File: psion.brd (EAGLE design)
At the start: 161.7 x 81.5 mm, 94 parts, among them J2 1-2295018-2, Q2 NTF3055L108T1G, Q3 NTF3055L108T1G, Q5 MOSFET-PCH_SOT-223, Q6 MOSFET-PCH_SOT-223, Q8 MMBT2907ALT1G, T1 2908-05WB-MG, U2 HV823LG-G, U3 ATMEGA32U4-AU, U4 OSD3358-512M-BCB, U5 MAX1620EEE+, U6 MAX1620EEE+, U7 ATTINY404-SSN, U8 TPS61090RSAR, Y1 ABM10-16.000MHZ-D30-T3

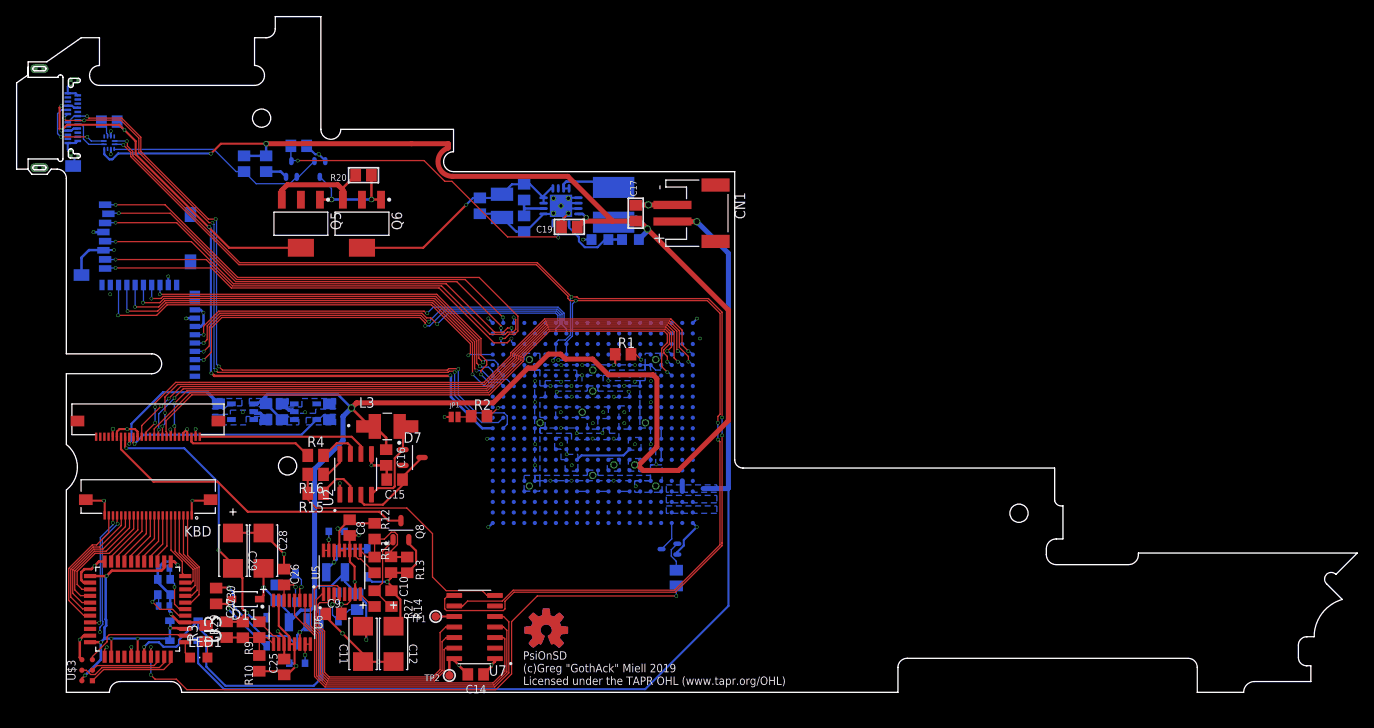
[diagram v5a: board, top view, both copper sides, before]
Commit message: Added audio compoments, massive board changes to accommodate physical space & rf restrictions
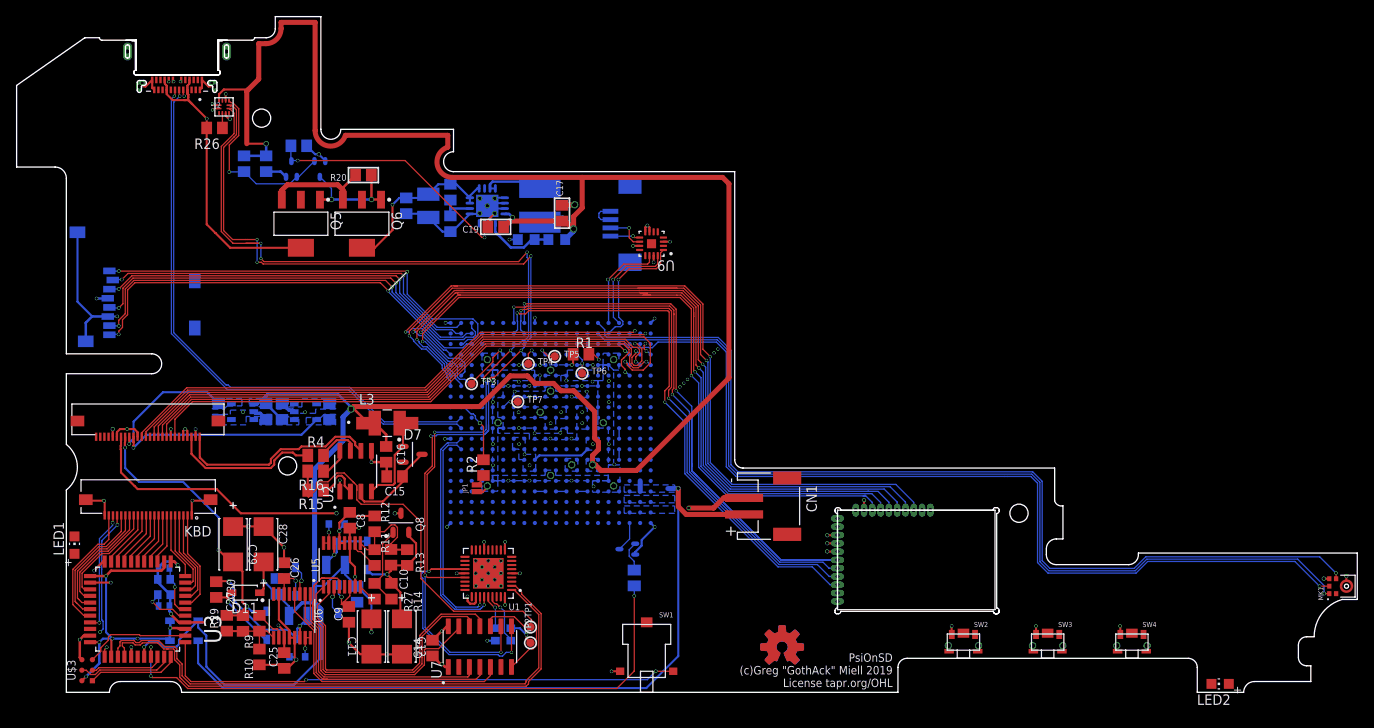
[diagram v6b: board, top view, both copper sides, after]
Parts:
- removed R3: 1k, adafruit:M0805
- added J1: 0522070433, gothack:MOLEX_0522070433
- added LED2: (no value), adafruit:CHIP-LED0805
- added MK1: SPH0645LM4H-B, gothack:MIC_SPH0645LM4H-B
- added SW1: KSM1131, gothack:KSM1131
- added SW2, SW3, SW4: LS12T2-T, gothack:LS12T2-T
- added TP3, TP4, TP5, TP6, TP7: (no value), microbuilder:TESTPOINT_ROUND_1MM
- added U1: USB2514BI-AEZG, USB2514BI-AEZG:QFN50P600X600X100-37N
- added U9: MAX98357AETE+, MAX98357AETE_:QFN50P300X300X80-17N
- added Y2: ABM10-24.000MHZ-E20-T, ABM10-16.000MHZ-D30-T3:XTAL250X200X50
- J2: device 1-2295018-2:TE_1-2295018-2 -> gothack:TE_1-2295018-2
- LED1: device adafruit:CHIPLED_0805 -> adafruit:CHIP-LED0805
- U$1: value LM832 -> LM832EMBEDDED; device LM832:LM832SMT -> gothack:LM832SMT_EMB
- moved U$1 82.1 mm to (99.0, 22.0), flipped to the top
- moved CN1 36.4 mm to (91.4, 22.5)
- moved U$5 28.5 mm to (92.3, 5.46)
- moved U$7 28.5 mm to (92.3, 5.46)
- moved LED1 20.2 mm to (6.99, 17.8), turned to 0 degrees
- moved J2 18.4 mm to (19.4, 77.3), flipped to the top, turned to 180 degrees
- moved U$4 14.5 mm to (25.0, 70.6), flipped to the top, turned to 0 degrees
- moved R26 12.7 mm to (23.9, 68.1), flipped to the top
- moved TP1 11.5 mm to (62.0, 7.87), turned to 90 degrees
- moved TP2 10.5 mm to (62.0, 5.97), turned to 90 degrees
- moved JP1 9.01 mm to (55.5, 24.6), turned to 90 degrees
- moved U8 8.89 mm to (56.8, 58.7)
- moved C17 8.89 mm to (65.8, 57.8)
- moved C18 8.89 mm to (47.0, 58.7)
- moved C19 8.89 mm to (57.8, 56.1)
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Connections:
- net LCD_BIASN_DN renamed LCD_BIASND_N
- net LCD_BIASP_DN renamed LCD_BIASPD_N
- net U0_CTS renamed UART0_CTS
- net U0_RTS renamed UART0_RTS
- net U0_RXD renamed UART0_RXD
- net U0_TXD renamed UART0_TXD
- net USBC_DN renamed USBCD_N
- net USBC_DP renamed USBCD_P
- removed net KBD_USB_DN: U3.3
- removed net KBD_USB_DP: U3.4
- removed net U1_CTS: U$1.P$18, U4.W8
- removed net U1_RTS: U$1.P$16, U4.Y8
- removed net U1_RXD: U$1.P$17, U4.Y7
- removed net U1_TXD: U$1.P$19, U4.W7
- removed net USB1_DN: U4.H2
- removed net USB1_DP: U4.J2
- new net AIN0: U4.Y10
- new net AIN1: U4.W10
- new net AIN2: U4.V10
- new net AIN3: U4.V9
- new net AIN4: U4.Y11
- new net AIN5: U4.W11
- new net AIN6: U4.V11
- new net AIN7: U4.V12
- new net ECAP0_IN_PWM0_OUT: U4.V15
- new net EMMC_RSTN: U4.A4
- new net EMU0: U4.V18
- new net EMU1: U4.V19
- new net EP: U9.17
- new net GPMC_A0: U4.A13
- new net GPMC_A1: U4.B13
- new net GPMC_A10: U4.B10
- new net GPMC_A11: U4.C10
- new net GPMC_A2: U4.C13
- new net GPMC_A3: U4.A12
- new net GPMC_A4: U4.B12
- new net GPMC_A5: U4.C12
- new net GPMC_A6: U4.A11
- new net GPMC_A7: U4.B11
- new net GPMC_A8: U4.C11
- new net GPMC_A9: U4.A10
- new net GPMC_AD10: U4.B16
- new net GPMC_AD11: U4.A16
- new net GPMC_AD12: U4.C15
- new net GPMC_AD13: U4.B15
- new net GPMC_AD14: U4.A15
- new net GPMC_AD15: U4.C14
- new net GPMC_AD8: U4.A17
- new net GPMC_AD9: U4.C16
- new net GPMC_ADVN_ALE: U4.L19
- new net GPMC_BEN0_CLE: U4.L20
- new net GPMC_BEN1: U4.C9
- new net GPMC_CLK: U4.A14
- new net GPMC_CSN0: U4.K20
- new net GPMC_CSN3: U4.B14
- new net GPMC_OEN_REN: U4.K19
- new net GPMC_WAIT0: U4.B9
- new net GPMC_WEN: U4.K18
- new net GPMC_WPN: U4.A9
- new net KBD_USBD_N: U1.1, U3.3
- new net KBD_USBD_P: U1.2, U3.4
- new net MCASP0_ACLKR: MK1.4, U4.Y15
- new net MCASP0_ACLKX: U4.Y17, U9.16
- new net MCASP0_AHCLKR: U4.W17
- new net MCASP0_AHCLKX: U4.V16
- new net MCASP0_AXR0: U4.W16, U9.1
- new net MCASP0_AXR1: MK1.6, U4.V17
- new net MCASP0_FSR: MK1.1, U4.W15
- new net MCASP0_FSX: U4.Y16, U9.14
- new net N$15: U1.32, Y2.3
- new net N$17: TP5.P$1, U4.U10
- new net N$18: TP6.P$1, U4.U13
- new net N$19: TP7.P$1, U4.M6
- new net N$20: J1.1, J1.2
- new net N$21: U3.6
- new net N$4: U1.33, Y2.1
- new net NC0: U4.A2
- new net NC1: U4.A3
- new net NC10: U4.B5
- new net NC11: U4.B6
- new net NC12: U4.B7
- new net NC13: U4.B8
- new net NC14: U4.C1
- new net NC15: U4.C2
- new net NC16: U4.C3
- new net NC17: U4.C4
- new net NC18: U4.C5
- new net NC19: U4.C6
- new net NC2: U4.A5
- new net NC20: U4.C7
- new net NC21: U4.C8
- new net NC22: U4.D1
- new net NC23: U4.D2
- new net NC24: U4.D3
- new net NC25: U4.D6
- new net NC26: U4.D7
- new net NC27: U4.D8
- new net NC28: U4.E1
- new net NC29: U4.E2
- new net NC3: U4.A6
- new net NC30: U4.E3
- new net NC31: U4.E18
- new net NC32: U4.F1
- new net NC33: U4.F2
- new net NC34: U4.F3
- new net NC35: U4.F4
- new net NC36: U4.F6
- new net NC37: U4.F7
- new net NC38: U4.F20
- new net NC39: U4.G1
- new net NC4: U4.A7
- new net NC40: U4.G2
- new net NC41: U4.U11
- new net NC42: U4.R17
- new net NC43: U4.R15
- new net NC44: U4.R14
- new net NC45: U4.R8
- new net NC46: U4.R7
- new net NC47: U4.R6
- new net NC48: U4.R4
- new net NC49: U4.P17
- new net NC5: U4.A8
- new net NC50: U4.P4
- new net NC51: U4.N17
- new net NC52: U4.N4
- new net NC53: U4.M17
- new net NC54: U4.M4
- new net NC55: U4.L17
- new net NC56: U4.L4
- new net NC57: U4.K4
- new net NC58: U4.J20
- new net NC59: U4.J19
- new net NC6: U4.B1
- new net NC60: U4.J18
- new net NC61: U4.J6
- new net NC62: U4.J4
- new net NC63: U4.H20
- new net NC64: U4.H19
- new net NC65: U4.H18
- new net NC66: U4.H13
- new net NC67: U4.H12
- new net NC68: U4.H11
- new net NC69: U4.H10
- new net NC7: U4.B2
- new net NC70: U4.H9
- new net NC71: U4.H6
- new net NC72: U4.H4
- new net NC73: U4.G20
- new net NC74: U4.G19
- new net NC75: U4.G18
- new net NC76: U4.G11
- new net NC77: U4.G10
- new net NC78: U4.G7
- new net NC79: U4.G6
- new net NC8: U4.B3
- new net NC80: U4.G4
- new net NC81: U4.G3
- new net NC9: U4.B4
- new net OSC0_CTL: U4.M1
- new net OSC1_GND: U4.W13
- new net OSC1_IN: U4.Y13
- new net OSC1_OUT: U4.Y14
- new net PMIC_MUX_IN: U4.F19
- new net PMIC_MUX_OUT: U4.U12
- new net PMIC_NRESET: U4.A19
- new net PMIC_TS: U4.E20
- new net PWRONRSTN_OD: U4.C17
- new net S: J1.S1, J1.S2
- new net SPI0_CS0: U4.Y4
- new net SPI0_CS1: U4.V4
- new net SPI0_D0: U4.W5
- new net SPI0_D1: U4.W4
- new net SPI0_SCLK: U4.Y5
- new net SPKR_LN: J1.3, U9.10
- new net SPKR_LP: J1.4, U9.9
- new net SW_LID: SW1.2, U3.12
- new net SW_MEDIA1: SW2.2
- new net SW_MEDIA2: SW3.2
- new net SW_MEDIA3: SW4.2
- new net SYS_ADC_1P8V: U4.Y12
- new net SYS_VDD1_CTL: U4.F18
- new net TCK: U4.Y19
- new net TDI: U4.Y18
- new net TDO: U4.W18
- new net TMS: U4.W19
- new net TRSTN: U4.W20
- new net UART1_CTS: U$1.18, U4.W8
- new net UART1_RTS: U$1.16, U4.Y8
- new net UART1_RXD: U$1.17, U4.Y7
- new net UART1_TXD: U$1.19, U4.W7
- new net USB1D_N: U1.30, U4.H2
- new net USB1D_P: U1.31, U4.J2
- new net USB1_CE: U4.J3
- new net USB1_DRVVBUS: U4.H3
- new net USB1_VBUS: U4.H1
- new net USBC_CE: U4.L3
- new net USBC_DRVVBUS: U4.K3
- new net USB_DN2D_N: U1.3
- new net USB_DN2D_P: U1.4
- new net USB_DN3D_N: U1.6
- new net USB_DN3D_P: U1.7
- new net USB_DN4D_N: U1.8
- new net USB_DN4D_P: U1.9
- new net VDDS_RTC@2: U4.U14
- new net VREFN: U4.W9
- new net VREFP: U4.W12
- new net WARMRSTN: U4.B17
- new net XDMA_EVENT_INTR0: U4.W14
- new net XDMA_EVENT_INTR1: U4.V14
- net +3V3: now also MK1.5, U$1.14, U$1.9, U1.10, U1.15, U1.23, U1.29, U1.36, U1.5, U9.7, U9.8; no longer U$1.P$14, U$1.P$9
- net GND: now also MK1.3, SW1.1, SW2.1, SW3.1, SW4.1, U$1.13, U$1.15, U1.37, U4.Y9, U9.11, U9.15, U9.3, Y2.2, Y2.4; no longer R3.2, U$1.P$13, U$1.P$15
- net I2C0_SCL: now also U1.24
- net I2C0_SDA: now also U1.22
- net KBDAVR_VCC: no longer U3.6
- net N$2: now also TP3.P$1, U4.U6; no longer LED1.C, R3.1
- net N$6: now also TP4.P$1, U4.U9; no longer LED1.A, U3.12
- net SD1_CLK: now also U$1.3; no longer U$1.P$3
- net SD1_CMD: now also U$1.5; no longer U$1.P$5
- net SD1_D0: now also U$1.6; no longer U$1.P$6
- net SD1_D1: now also U$1.8; no longer U$1.P$8
- net SD1_D2: now also U$1.4; no longer U$1.P$4
- net SD1_D3: now also U$1.7; no longer U$1.P$7
- net USBC_ID: now also U4.L1
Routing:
- net MCASP0_ACLKR: track 0.00 -> 117.4 mm, vias 0 -> 1
- net MCASP0_FSR: track 0.00 -> 116.6 mm, vias 0 -> 1
- net MCASP0_AXR1: track 0.00 -> 113.3 mm, vias 0 -> 1
- net UART1_RTS: track 0.00 -> 93.2 mm, vias 0 -> 2
- net KBD_USBD_P: track 0.00 -> 69.1 mm
- net KBD_USBD_N: track 0.00 -> 68.3 mm
- net UART1_TXD: track 0.00 -> 66.0 mm, vias 0 -> 2
- net UART1_CTS: track 0.00 -> 65.3 mm, vias 0 -> 2
- net UART1_RXD: track 0.00 -> 64.7 mm, vias 0 -> 2
- net SW_LID: track 0.00 -> 63.7 mm, vias 0 -> 2
- net USBC_VBUS: track 101.1 -> 37.6 mm, vias 6 -> 1
- net U1_TXD: track 51.9 -> 0.00 mm, vias 2 -> 0
- net U1_CTS: track 51.2 -> 0.00 mm, vias 2 -> 0
- net U1_RXD: track 48.5 -> 0.00 mm, vias 2 -> 0
- net U1_RTS: track 48.3 -> 0.00 mm, vias 2 -> 0
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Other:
- outline, holes or cut-outs redrawn
- board text added: "PsiOnSD (c)Greg "GothAck" Miell 2019 License tapr.org/OHL"
- board text removed: "PsiOnSD (c)Greg "GothAck" Miell 2019 Licensed under the TAPR OHL (www.tapr.org/OHL)"

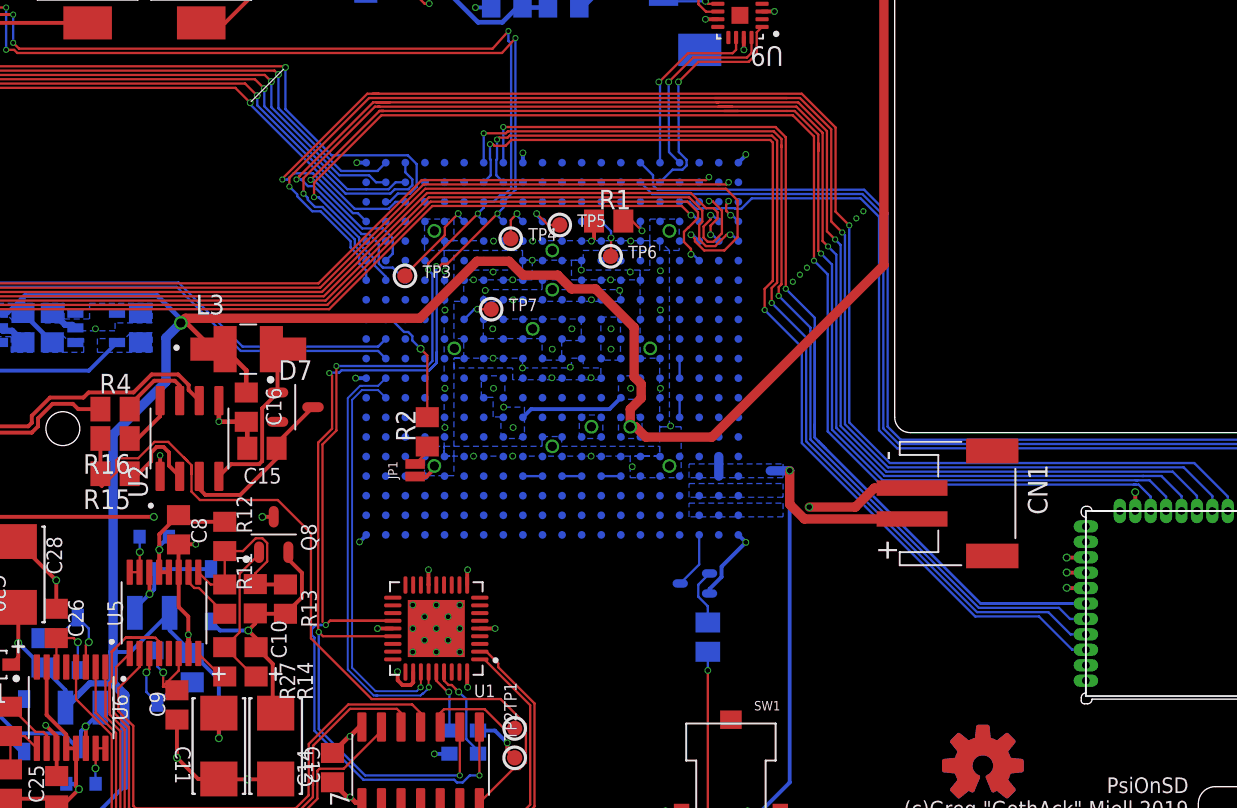
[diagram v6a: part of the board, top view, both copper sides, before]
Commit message: Cleared some DRC issues
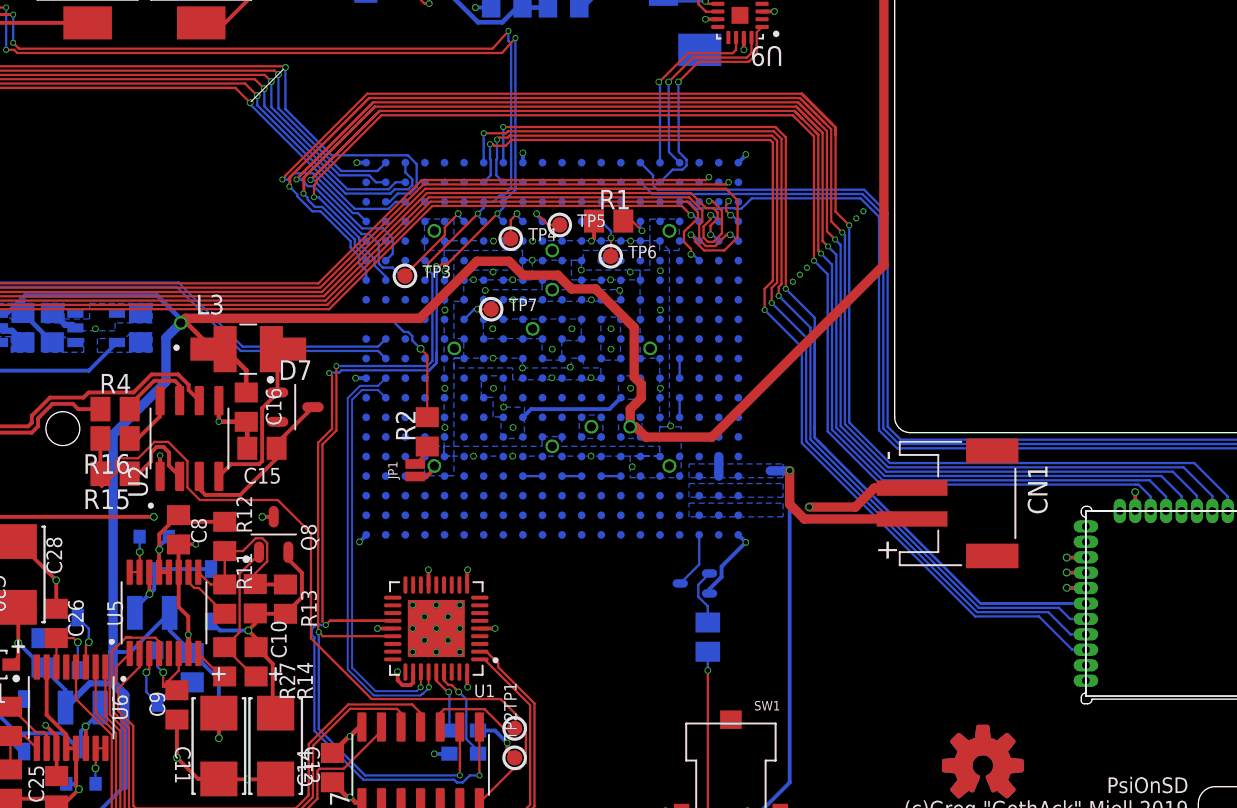
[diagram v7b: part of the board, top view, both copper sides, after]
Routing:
- net SD1_D0: track 89.4 -> 99.1 mm
- net SD1_CMD: track 94.2 -> 103.7 mm
- net SD1_D3: track 89.7 -> 95.8 mm
- net SD1_CLK: track 93.4 -> 99.3 mm
- net SD1_D2: track 98.0 -> 103.5 mm
- net LCD_BIASP_SHDN_: track 40.1 -> 36.5 mm
- net LCD_EL_EN: track 52.3 -> 51.5 mm

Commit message: more drc issues
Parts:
- moved R4 0.36 mm to (36.1, 28.9)
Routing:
- net I2C0_SDA: track 138.6 -> 131.8 mm
- net GND: track 175.4 -> 173.0 mm
